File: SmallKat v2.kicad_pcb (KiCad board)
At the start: 4 copper layers, 100 x 56 mm, 153 parts, among them IC1 LMR14010A, IC2 LMR14010A, IC3 TPS40192DRCT-TPS40192DRCT, J1 Qwiic connector, J10 Conn_01x03_Male, J11 Conn_01x03_Male, J12 Conn_01x03_Male, J13 Conn_01x03_Male, J14 Conn_01x03_Male, J15 Conn_01x03_Male, J16 Conn_01x03_Male, J17 Conn_01x03_Male, J18 Conn_01x03_Male, J19 Conn_01x03_Male, J2 Qwiic connector, J20 Conn_01x03_Male, J21 Conn_01x03_Male, J22 Conn_01x03_Male, J23 Conn_01x03_Male, J24 Conn_01x03_Male, J25 Conn_01x02_Female, J3 Conn_01x03_Male, J4 Conn_01x03_Male, J5 Conn_01x03_Male, J6 Conn_01x03_Male, J7 Micro_SD_Card, J8 USB_C_Receptacle, J9 Conn_01x03_Male, Q1 MBT3904DW1, Q2 BUK9M17-30EX / BUK7M10-40E, Q3 BUK9M17-30EX / BUK7M10-40E, SW1 SW_SPST, SW2 SW_SPST, U1 PCA9685BS, U2 BNO055, U3 ESP32-WROOM-32, U4 CP2102N-A01-GQFN24, Y1 32.768kHz

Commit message: Ready to order
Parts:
- added TP14: TestPoint, TestPoint:TestPoint_Pad_D1.5mm, B.Cu at (105.1, 114.4)
- added TP15: TestPoint, TestPoint:TestPoint_Pad_D1.5mm, B.Cu at (96.0, 102.8)
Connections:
- U1 pad 22: (no net) -> GND
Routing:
- net /MainBoard/ESP32Module/EN: track 23.1 -> 25.6 mm, vias 4 -> 5
- net /MainBoard/ESP32Module/IO0: track 43.9 -> 45.4 mm
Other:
- board text added: "Board by: Keion Bisland 2021"
- board text added: "I2C_1"
- board text added: "I2C_2"
- board text added: "IO0"
- board text removed: "Board by: Keion Bisland 2020"

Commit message: Update README.md
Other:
- board text added: "+"
- board text added: "-"
- board text added: "<- Head"
- board text added: "I2C 1"
- board text added: "I2C 2"
- board text added: "Rev 1.0"
- board text added: "Tail ->"
- board text removed: "I2C_1"
- board text removed: "I2C_2"
- board text removed: "Rev ??"

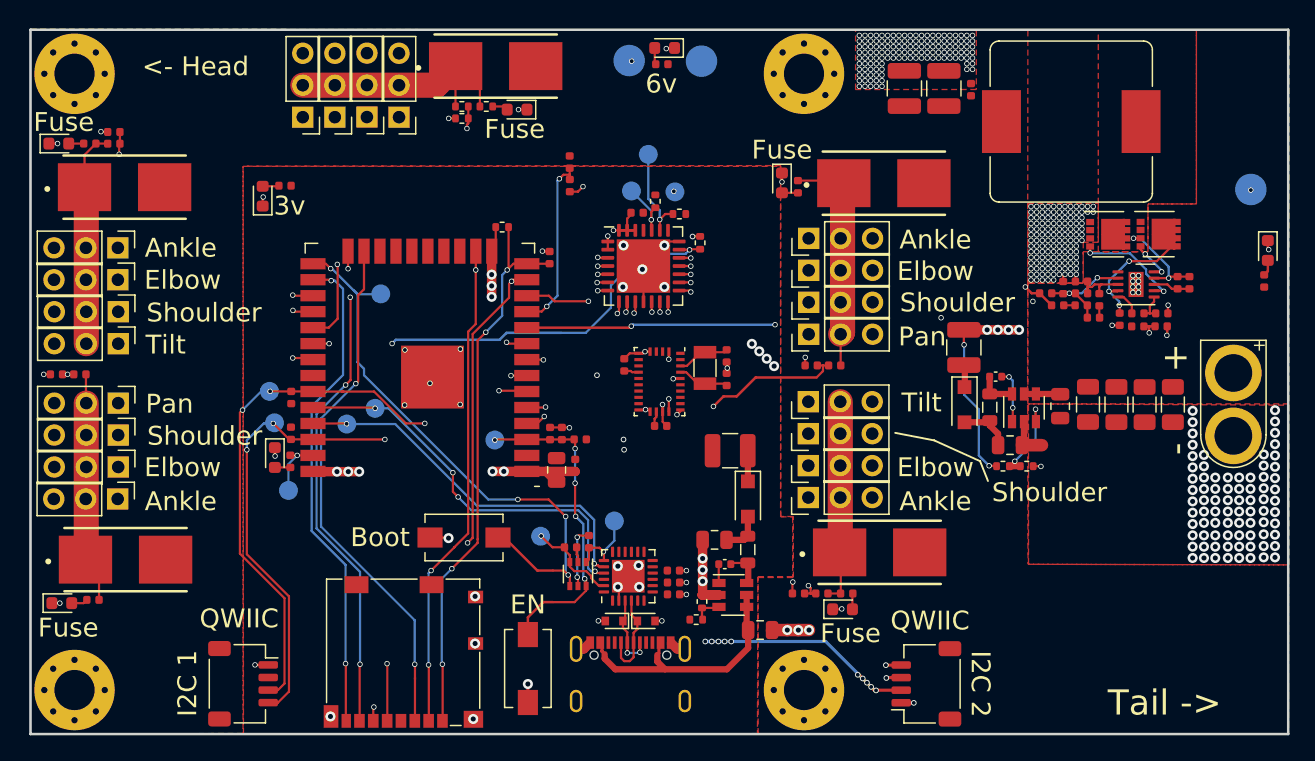
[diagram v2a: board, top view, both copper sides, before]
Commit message: ordered version with foot connecotrs
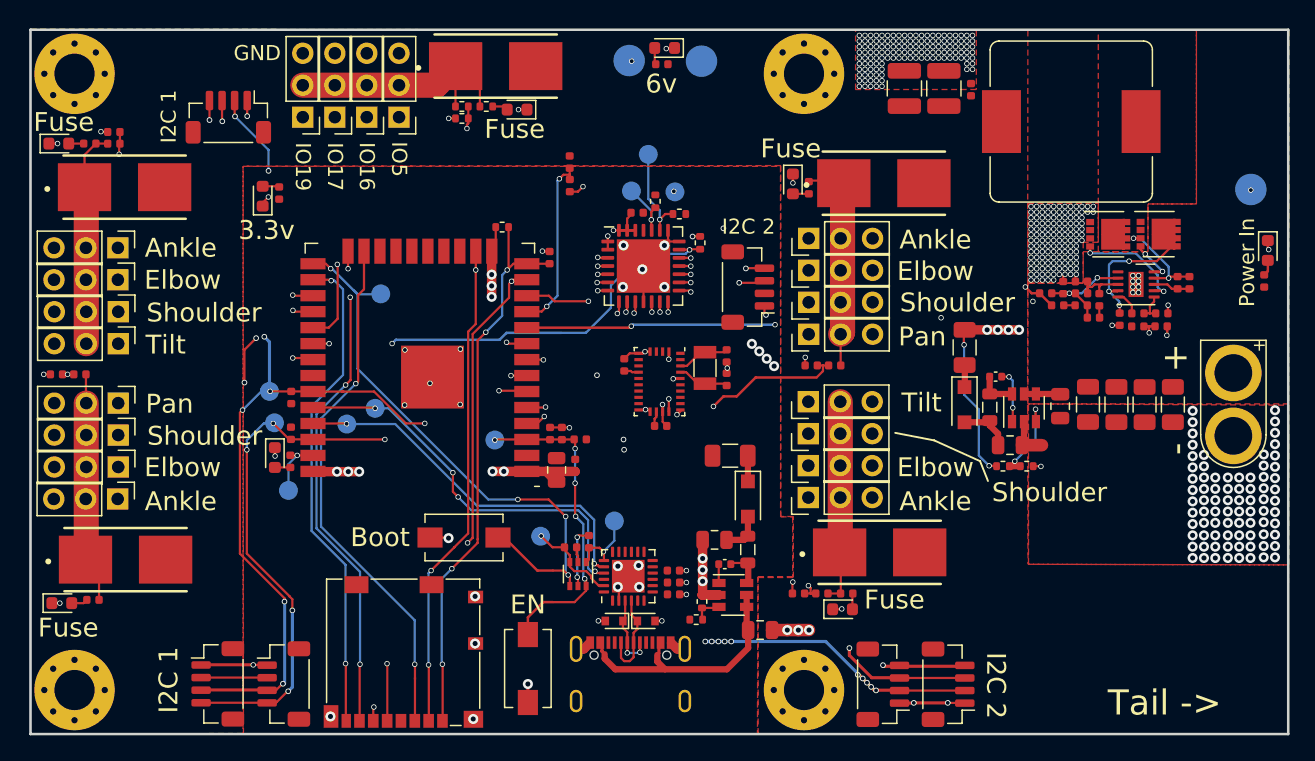
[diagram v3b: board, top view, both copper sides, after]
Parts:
- added J26: Qwiic connector, Connector_JST:JST_SH_BM04B-SRSS-TB_1x04-1MP_P1.00mm_Vertical, F.Cu at (125.2, 102.3)
- added J27: Qwiic connector, Connector_JST:JST_SH_BM04B-SRSS-TB_1x04-1MP_P1.00mm_Vertical, F.Cu at (141.1, 133.8)
- added J28: Qwiic connector, Connector_JST:JST_SH_BM04B-SRSS-TB_1x04-1MP_P1.00mm_Vertical, F.Cu at (83.0, 133.8)
- added J29: Qwiic connector, Connector_JST:JST_SH_BM04B-SRSS-TB_1x04-1MP_P1.00mm_Vertical, F.Cu at (83.9, 88.8)
- F6, F7: footprint Fuse:Fuse_1210_3225Metric -> Fuse:Fuse_1206_3216Metric
- J1, J2: footprint Connector_JST:JST_SH_SM04B-SRSS-TB_1x04-1MP_P1.00mm_Horizontal -> Connector_JST:JST_SH_BM04B-SRSS-TB_1x04-1MP_P1.00mm_Vertical
- moved J1 3.46 mm to (135.9, 133.8)
- moved J2 3.24 mm to (88.3, 133.8)
- moved R35 0.87 mm to (130.0, 94.4)
- moved D12 0.87 mm to (128.8, 94.1)
- moved R16 0.75 mm to (87.9, 94.8), turned to 90 degrees
- moved F7 0.40 mm to (123.8, 115.7)
- moved F6 0.06 mm to (142.4, 107.1)
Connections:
- J1 pad 3: /MainBoard/SCL_1 -> /MainBoard/SDA_1
- J1 pad 4: /MainBoard/SDA_1 -> /MainBoard/SCL_1
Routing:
- net /MainBoard/SCL: track 60.8 -> 95.0 mm, vias 4 -> 9
- net /MainBoard/SDA: track 63.1 -> 93.1 mm, vias 4 -> 8
- net /MainBoard/SDA_1: track 60.8 -> 79.6 mm, vias 5 -> 7
- net +3V3: track 59.3 -> 76.5 mm, vias 21 -> 23
- net /MainBoard/SCL_1: track 66.2 -> 82.2 mm, vias 4 -> 5
- net GND: track 80.2 -> 91.6 mm, vias 427 -> 430
- net /MainBoard/Servos/6V4: track 18.5 -> 17.7 mm
- net +BATT: track 14.2 -> 15.0 mm
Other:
- board text added: "Head ->"
- board text added: "IO16"
- board text added: "IO17"
- board text added: "IO19"
- board text added: "IO5"
- board text added: "Power In"
- board text removed: "3v"
- board text removed: "<- Head"
- board text removed: "QWIIC"

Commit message: fully routed, currently 4 layers, ordered 2 layer version with only middle 2 layers removed
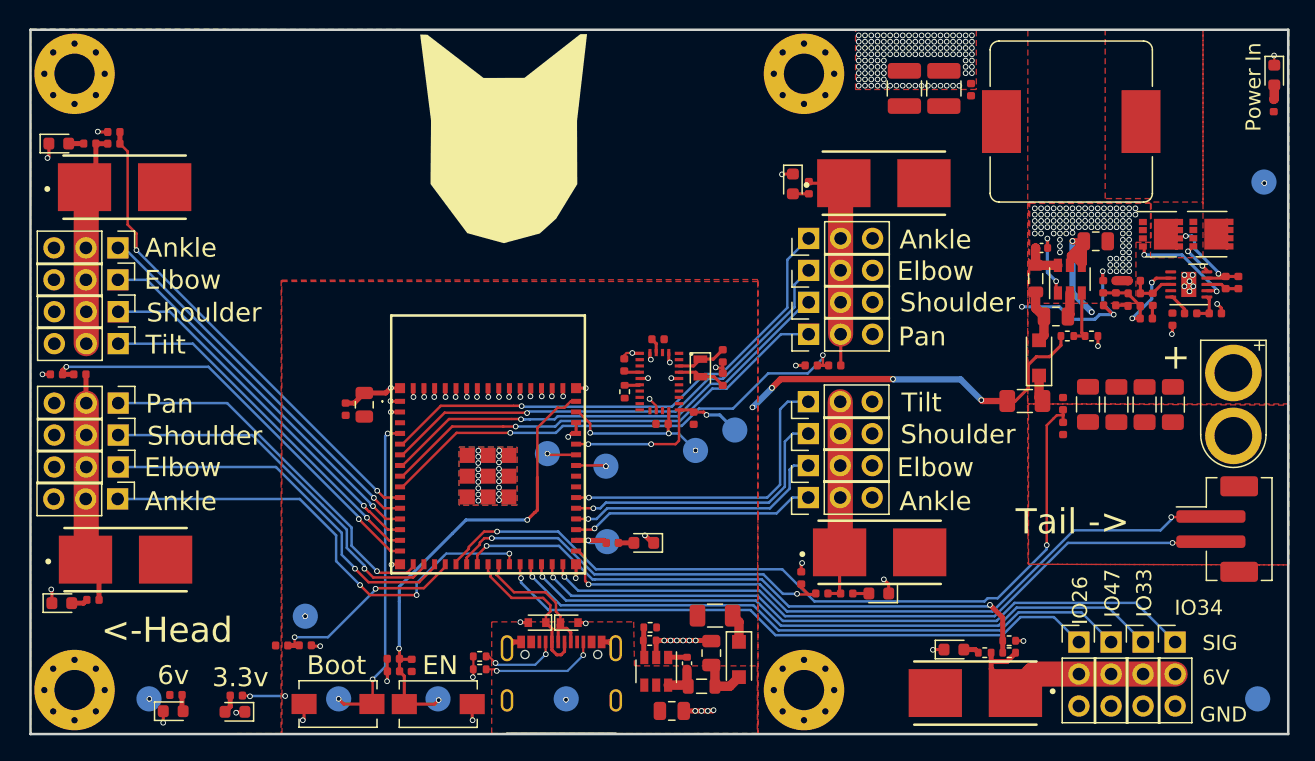
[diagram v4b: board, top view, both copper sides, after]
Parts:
- removed C1, C20, C21: 0.1uF, Capacitor_SMD:C_0402_1005Metric
- removed C19: 4.7uF, Capacitor_SMD:C_0402_1005Metric
- removed J2, J26, J27, J28, J29: Qwiic connector, Connector_JST:JST_SH_BM04B-SRSS-TB_1x04-1MP_P1.00mm_Vertical
- removed J7: Micro_SD_Card, Connector_Card:microSD_HC_Molex_104031-0811
- removed Q1: MBT3904DW1, Package_TO_SOT_SMD:SOT-363_SC-70-6
- removed R21, R22, R44, R45, R46: 10K, Resistor_SMD:R_0402_1005Metric
- removed TP12: SDA, TestPoint:TestPoint_Pad_D1.5mm
- removed TP13: SCL, TestPoint:TestPoint_Pad_D1.5mm
- removed TP8: TestPoint, TestPoint:TestPoint_Pad_D1.5mm
- removed U1: PCA9685BS, Package_DFN_QFN:QFN-28-1EP_6x6mm_P0.65mm_EP4.25x4.25mm
- removed U2: BNO055, Package_LGA:LGA-28_5.2x3.8mm_P0.5mm
- removed U3: ESP32-WROOM-32, RF_Module:ESP32-WROOM-32
- removed U4: CP2102N-A01-GQFN24, Package_DFN_QFN:QFN-24-1EP_4x4mm_P0.5mm_EP2.6x2.6mm
- added AC1: BNO085, BNO085:BNO085, F.Cu at (118.2, 109.8)
- added G***: LOGO, Smallkat_Logo:logo, F.Cu at (105.7, 90.8)
- added G***: LOGO, Smallkat_Logo:logo, B.Cu at (106.2, 101.3)
- added IC4: ESP32-S3-MINI-1-N8, ESP32-s3-wroom-mini:ESP32S3MINI1N8, F.Cu at (104.5, 114.8)
- added R15: 10K, Resistor_SMD:R_0402_1005Metric, F.Cu at (115.4, 110.6)
- added REF**: KiCad-Logo2_5mm_SilkScreen, Symbol:KiCad-Logo2_5mm_SilkScreen, B.Cu at (140.7, 134.1)
- added REF**: OSHW-Logo2_9.8x8mm_SilkScreen, Symbol:OSHW-Logo2_9.8x8mm_SilkScreen, B.Cu at (140.8, 125.8)
- J1: value Qwiic connector -> BATT_SERIAL; footprint Connector_JST:JST_SH_BM04B-SRSS-TB_1x04-1MP_P1.00mm_Vertical -> Connector_JST:JST_PH_B2B-PH-SM4-TB_1x02-1MP_P2.00mm_Vertical
- R14, R18: value 10K -> 5.1K
- TP1, TP14, TP15, TP2, TP3, TP4, TP5, TP6, TP7: footprint TestPoint:TestPoint_Pad_D1.5mm -> TestPoint:TestPoint_Pad_D2.0mm
- TP10, TP11, TP9: footprint TestPoint:TestPoint_Pad_D2.5mm -> TestPoint:TestPoint_Pad_D2.0mm
- Y1: footprint Crystal:Crystal_SMD_3215-2Pin_3.2x1.5mm -> Crystal:Crystal_SMD_2012-2Pin_2.0x1.2mm
- moved J6 81.0 mm to (159.2, 130.5), turned to 0 degrees
- moved J4 76.6 mm to (156.6, 130.5), turned to 0 degrees
- moved J5 72.4 mm to (154.1, 130.5), turned to 0 degrees
- moved J3 68.3 mm to (151.5, 130.5), turned to 0 degrees
- moved TP10 67.3 mm to (165.7, 135.0), turned to 180 degrees
- moved D13 65.6 mm to (79.5, 136.0), turned to 0 degrees
- moved TP11 63.5 mm to (77.6, 135.0), turned to 180 degrees
- moved R43 63.3 mm to (79.7, 134.7), turned to 0 degrees
- moved F1 62.8 mm to (143.3, 134.5), turned to 180 degrees
- moved R7 61.5 mm to (146.0, 131.3), turned to 180 degrees
- moved R8 60.1 mm to (146.0, 130.4), turned to 0 degrees
- moved R9 58.8 mm to (144.0, 131.3), turned to 180 degrees
- moved D3 55.2 mm to (141.6, 131.1), turned to 0 degrees
- moved TP4 44.7 mm to (90.0, 128.4), turned to 180 degrees
- moved R4 44.7 mm to (88.1, 130.8), turned to 0 degrees
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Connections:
- net /MainBoard/ESP32Module/IO23 renamed /MainBoard/ESP32Module/IO36
- IC3 pad 1: (no net) -> unconnected-(IC3-Pad1)
- J1 pad 1: GND -> /MainBoard/BATT_SERIAL_TX
- J1 pad 2: +3V3 -> /MainBoard/BATT_SERIAL_RX
- J8 pad A5: (no net) -> Net-(J8-PadA5)
- J8 pad A8: (no net) -> unconnected-(J8-PadA8)
- J8 pad B5: (no net) -> Net-(J8-PadB5)
- J8 pad B8: (no net) -> unconnected-(J8-PadB8)
- R14 pad 1: /MainBoard/EN_SERVO_DRIVER -> GND
- R14 pad 2: GND -> Net-(J8-PadA5)
- R17 pad 1: Net-(R17-Pad1) -> +3V3
- R17 pad 2: GND -> Net-(AC1-Pad4)
- R18 pad 1: /MainBoard/IO12 -> GND
- R18 pad 2: GND -> Net-(J8-PadB5)
- TP7 pad 1: /MainBoard/ESP32Module/DTR -> VBUS
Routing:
- net /MainBoard/SCL_1: track 82.2 -> 0.00 mm, vias 5 -> 0
- net /MainBoard/SCL: track 95.0 -> 13.0 mm, vias 9 -> 3
- net /MainBoard/SDA_1: track 79.6 -> 0.00 mm, vias 7 -> 0
- net /MainBoard/SDA: track 93.1 -> 15.9 mm, vias 8 -> 3
- net /MainBoard/BATT_SERIAL_TX: track 0.00 -> 56.8 mm, vias 0 -> 2
- net /MainBoard/BATT_SERIAL_RX: track 0.00 -> 56.2 mm, vias 0 -> 2
- net /MainBoard/IO12: track 45.1 -> 0.00 mm, vias 4 -> 0
- net +3V3: track 76.5 -> 33.2 mm, vias 23 -> 7
- net /MainBoard/IO15: track 42.0 -> 0.00 mm, vias 2 -> 0
- net /MainBoard/IO14: track 40.3 -> 0.00 mm, vias 3 -> 0
- net /MainBoard/IO2: track 40.0 -> 0.00 mm, vias 4 -> 0
- net /MainBoard/IO4: track 39.2 -> 0.00 mm, vias 2 -> 0
- net /MainBoard/IO13: track 38.9 -> 0.00 mm, vias 3 -> 0
- net /MainBoard/EN_SERVO_DRIVER: track 35.8 -> 0.00 mm, vias 3 -> 0
- net /MainBoard/AD_SERVO_3: track 19.4 -> 52.1 mm
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- added copper zone on In1.Cu, net +3V3
- added copper zone on In1.Cu, net GND
- added copper zone on F.Cu, net VBUS
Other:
- net class Default removed
- board text added: "6V"
- board text added: "<-Head"
- board text added: "IO 36"
- board text added: "IO26"
- board text added: "IO33"
- board text added: "IO34"
- board text added: "IO47"
- board text added: "SIG"
- board text added: "VBUS"
- board text removed: "-"
- board text removed: "Board by: Keion Bisland 2021"
- board text removed: "DTR"
- board text removed: "Fuse"
- board text removed: "Head ->"
- board text removed: "I2C 1"
- board text removed: "I2C 2"
- board text removed: "IO 23"
- board text removed: "IO16"
- board text removed: "IO17"
- board text removed: "IO19"
- board text removed: "IO5"
- board text removed: "RTS"
- board text removed: "SCL 1"
- board text removed: "SDA 1"
